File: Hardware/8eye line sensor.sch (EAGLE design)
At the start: 78 parts, among them U1 SX1509, U101 QRE1113, U102 QRE1113, U103 QRE1113, U104 QRE1113, U105 QRE1113, U106 QRE1113, U107 QRE1113, U108 QRE1113, U2 74AC125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

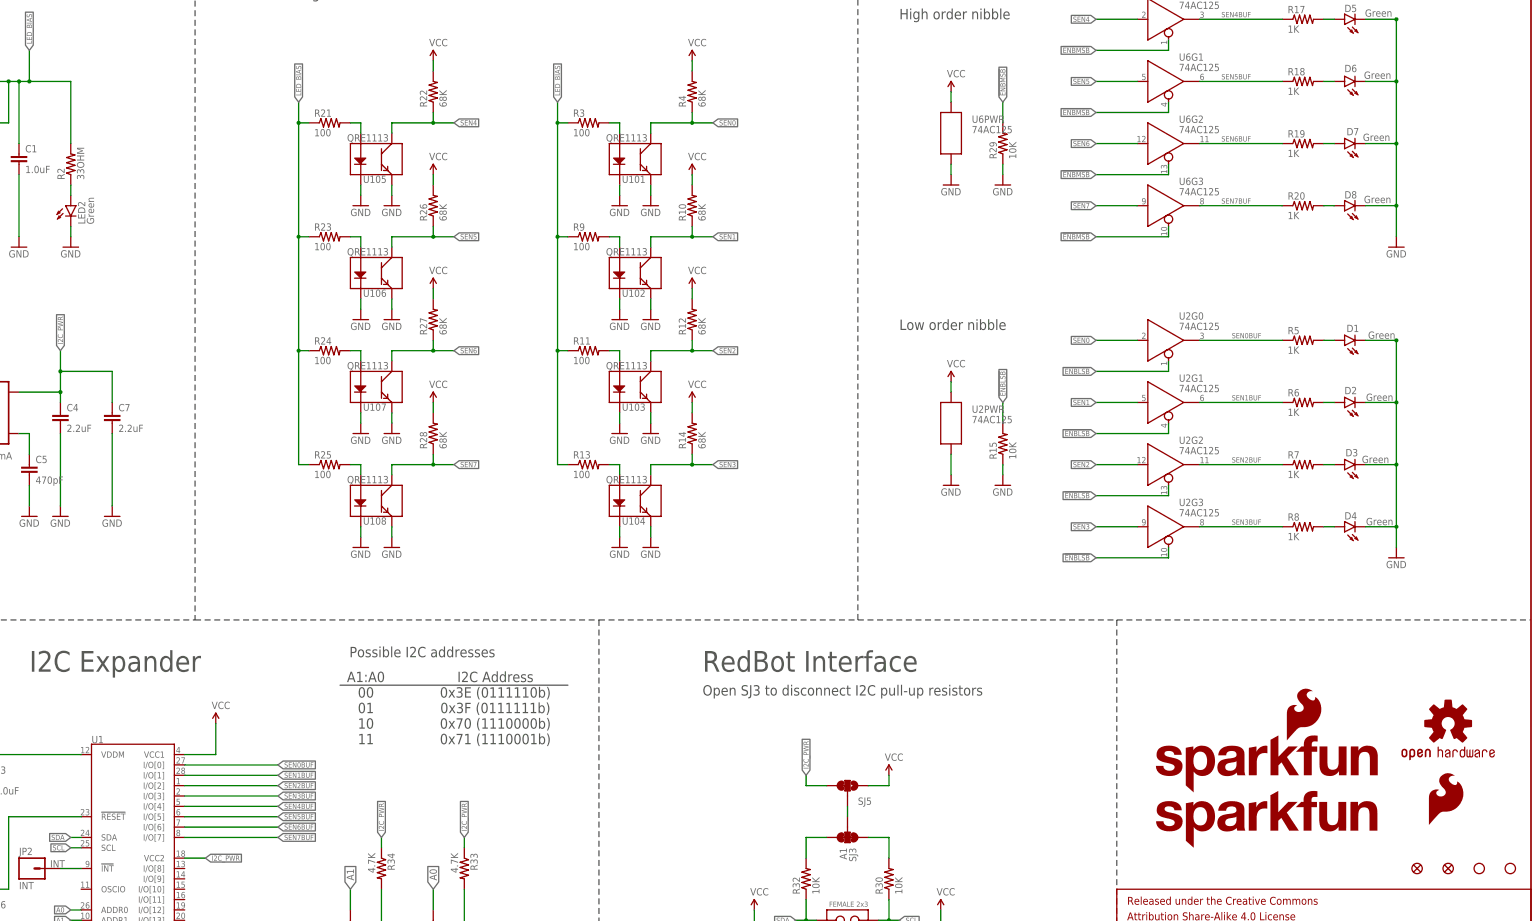
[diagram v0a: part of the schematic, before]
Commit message: Fixed github/qc finds
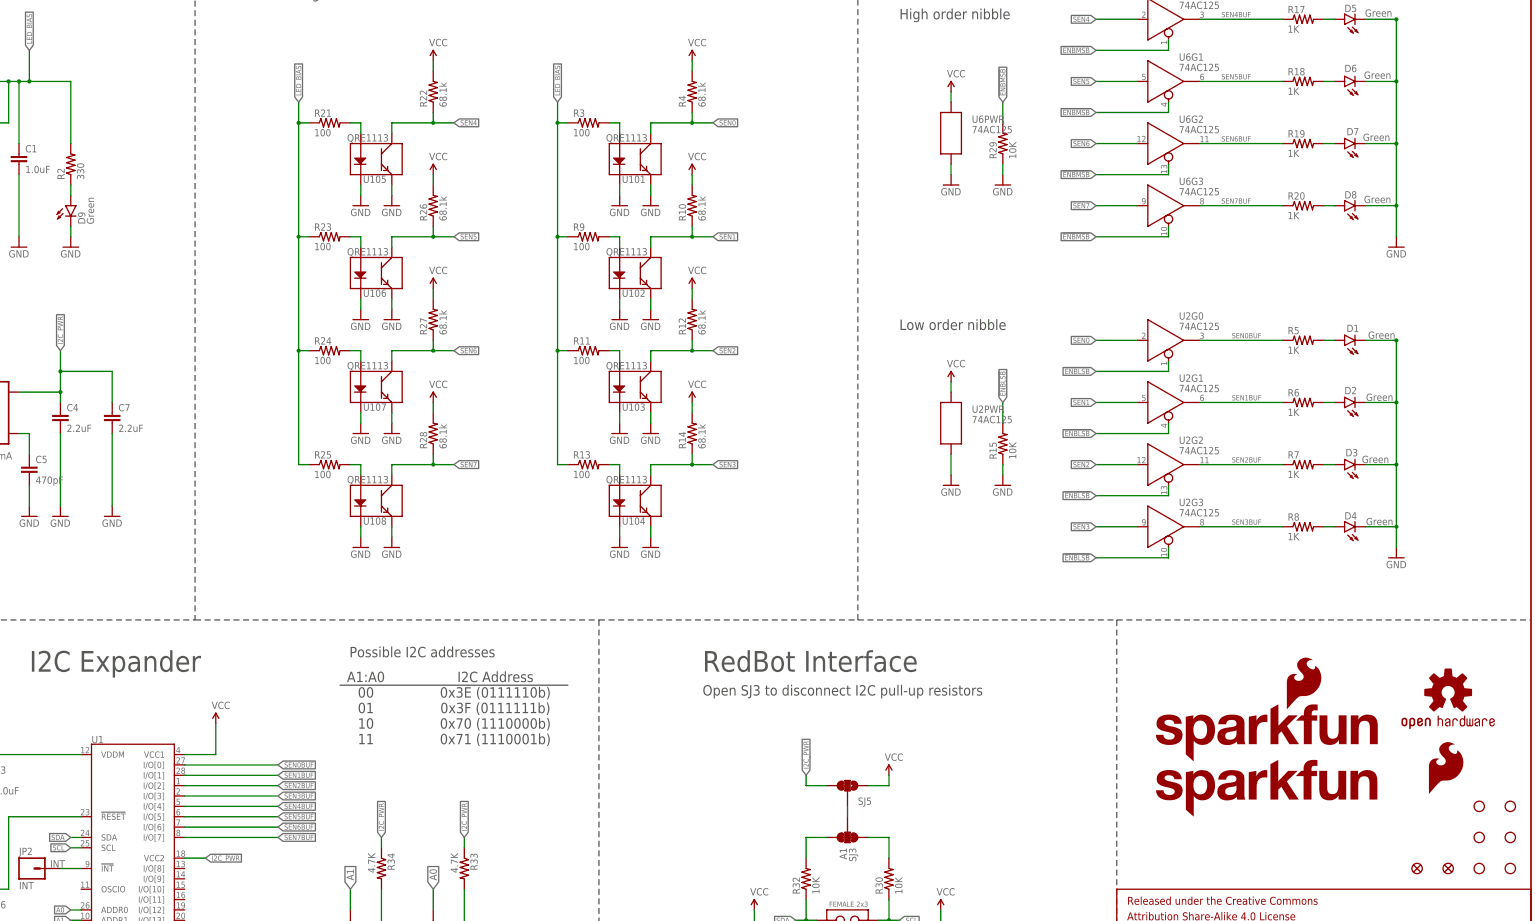
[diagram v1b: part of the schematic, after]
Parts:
- added STANDOFF1, STANDOFF2, STANDOFF5, STANDOFF6: STAND-OFF, SparkFun-Electromechanical:STAND-OFF
- R10, R12, R14, R22, R26, R27, R28, R4: value 68K -> 68.1k
- R2: value 33OHM -> 330; device SparkFun-Resistors:33OHM1/10W1%(0603) -> SparkFun-Resistors:330OHM1/10W1%(0603)
- renumbered LED2 to D9
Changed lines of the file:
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@@
 <part name="R1" library="SparkFun-Resistors" deviceset="4.7KOHM-1/10W-1%(0603)" device="" value="4.7K"/>
 <part name="R3" library="SparkFun-Resistors" deviceset="100OHM-1/10W-1%(0603)" device="" value="100"/>
-<part name="R4" library="SparkFun-Resistors" deviceset="68.1KOHM1/10W1%(0603)" device="" value="68K"/>
+<part name="R4" library="SparkFun-Resistors" deviceset="68.1KOHM1/10W1%(0603)" device="" value="68.1k"/>
 <part name="GND1" library="SparkFun-Aesthetics" deviceset="GND" device=""/>
 <part name="GND2" library="SparkFun-Aesthetics" deviceset="GND" device=""/>
@@
 <part name="GND12" library="SparkFun-Aesthetics" deviceset="GND" device=""/>
 <part name="SUPPLY2" library="SparkFun-Aesthetics" deviceset="VCC" device=""/>
-<part name="R10" library="SparkFun-Resistors" deviceset="68.1KOHM1/10W1%(0603)" device="" value="68K"/>
+<part name="R10" library="SparkFun-Resistors" deviceset="68.1KOHM1/10W1%(0603)" device="" value="68.1k"/>
 <part name="SUPPLY3" library="SparkFun-Aesthetics" deviceset="VCC" device=""/>
-<part name="R12" library="SparkFun-Resistors" deviceset="68.1KOHM1/10W1%(0603)" device="" value="68K"/>
+<part name="R12" library="SparkFun-Resistors" deviceset="68.1KOHM1/10W1%(0603)" device="" value="68.1k"/>
 <part name="SUPPLY4" library="SparkFun-Aesthetics" deviceset="VCC" device=""/>
-<part name="R14" library="SparkFun-Resistors" deviceset="68.1KOHM1/10W1%(0603)" device="" value="68K"/>
+<part name="R14" library="SparkFun-Resistors" deviceset="68.1KOHM1/10W1%(0603)" device="" value="68.1k"/>
 <part name="SUPPLY5" library="SparkFun-Aesthetics" deviceset="VCC" device=""/>
 <part name="SUPPLY6" library="SparkFun-Aesthetics" deviceset="VCC" device=""/>
@@
 <part name="R15" library="SparkFun-Resistors" deviceset="10KOHM-1/10W-1%(0603)" device="0603" value="10K"/>
 <part name="R16" library="SparkFun-Electromechanical" deviceset="TRIMPOT" device="-PTH-KNOB" value="TSR-3386"/>
-<part name="R2" library="SparkFun-Resistors" deviceset="33OHM1/10W1%(0603)" device="" value="33OHM"/>
-<part name="LED2" library="SparkFun-LED" deviceset="LED-GREEN" device="1206-BOTTOM" value="Green"/>
+<part name="R2" library="SparkFun-Resistors" deviceset="330OHM1/10W1%(0603)" device="" value="330"/>
+<part name="D9" library="SparkFun-LED" deviceset="LED-GREEN" device="1206-BOTTOM" value="Green"/>
 <part name="GND16" library="SparkFun" deviceset="GND" device=""/>
 <part name="GND17" library="SparkFun-Aesthetics" deviceset="GND" device=""/>
@@
 <part name="U105" library="SparkFun-Sensors" deviceset="QRE1113" device="" value="QRE1113"/>
 <part name="R21" library="SparkFun-Resistors" deviceset="100OHM-1/10W-1%(0603)" device="" value="100"/>
-<part name="R22" library="SparkFun-Resistors" deviceset="68.1KOHM1/10W1%(0603)" device="" value="68K"/>
+<part name="R22" library="SparkFun-Resistors" deviceset="68.1KOHM1/10W1%(0603)" device="" value="68.1k"/>
 <part name="GND19" library="SparkFun-Aesthetics" deviceset="GND" device=""/>
 <part name="GND20" library="SparkFun-Aesthetics" deviceset="GND" device=""/>
@@
 <part name="GND26" library="SparkFun-Aesthetics" deviceset="GND" device=""/>
 <part name="SUPPLY9" library="SparkFun-Aesthetics" deviceset="VCC" device=""/>
-<part name="R26" library="SparkFun-Resistors" deviceset="68.1KOHM1/10W1%(0603)" device="" value="68K"/>
+<part name="R26" library="SparkFun-Resistors" deviceset="68.1KOHM1/10W1%(0603)" device="" value="68.1k"/>
 <part name="SUPPLY10" library="SparkFun-Aesthetics" deviceset="VCC" device=""/>
-<part name="R27" library="SparkFun-Resistors" deviceset="68.1KOHM1/10W1%(0603)" device="" value="68K"/>
+<part name="R27" library="SparkFun-Resistors" deviceset="68.1KOHM1/10W1%(0603)" device="" value="68.1k"/>
 <part name="SUPPLY11" library="SparkFun-Aesthetics" deviceset="VCC" device=""/>
-<part name="R28" library="SparkFun-Resistors" deviceset="68.1KOHM1/10W1%(0603)" device="" value="68K"/>
+<part name="R28" library="SparkFun-Resistors" deviceset="68.1KOHM1/10W1%(0603)" device="" value="68.1k"/>
 <part name="SUPPLY12" library="SparkFun-Aesthetics" deviceset="VCC" device=""/>
 <part name="SJ1" library="SparkFun-Passives" deviceset="JUMPER-PAD-3-2OF3_NC_BY_PASTE" device="" value="A0"/>
@@
 <part name="FID1" library="SparkFun-Aesthetics" deviceset="FIDUCIAL" device="UFIDUCIAL"/>
 <part name="FID2" library="SparkFun-Aesthetics" deviceset="FIDUCIAL" device="UFIDUCIAL"/>
-<part name="STANDOFF3" library="SparkFun-Electromechanical" deviceset="STAND-OFF" device=""/>
-<part name="STANDOFF4" library="SparkFun-Electromechanical" deviceset="STAND-OFF" device=""/>
 <part name="U6" library="SparkFun-DigitalIC" deviceset="74*125" device="" technology="AC125DG" value="74AC125"/>
 <part name="U2" library="SparkFun-DigitalIC" deviceset="74*125" device="" technology="AC125DG" value="74AC125"/>
@@
 <part name="R34" library="SparkFun-Resistors" deviceset="4.7KOHM-1/10W-1%(0603)" device="" value="4.7K"/>
 <part name="LOGO1" library="SparkFun-Aesthetics" deviceset="SFE_LOGO_NAME_FLAME" device=".2_INCH"/>
+<part name="STANDOFF1" library="SparkFun-Electromechanical" deviceset="STAND-OFF" device=""/>
+<part name="STANDOFF2" library="SparkFun-Electromechanical" deviceset="STAND-OFF" device=""/>
+<part name="STANDOFF3" library="SparkFun-Electromechanical" deviceset="STAND-OFF" device=""/>
+<part name="STANDOFF4" library="SparkFun-Electromechanical" deviceset="STAND-OFF" device=""/>
+<part name="STANDOFF5" library="SparkFun-Electromechanical" deviceset="STAND-OFF" device=""/>
+<part name="STANDOFF6" library="SparkFun-Electromechanical" deviceset="STAND-OFF" device=""/>
 </parts>
 <sheets>
@@
 </instance>
 <instance part="R2" gate="G$1" x="73.66" y="213.36" rot="R90"/>
-<instance part="LED2" gate="G$1" x="73.66" y="203.2"/>
+<instance part="D9" gate="G$1" x="73.66" y="203.2"/>
 <instance part="GND16" gate="1" x="73.66" y="193.04"/>
 <instance part="GND17" gate="1" x="398.78" y="193.04"/>
@@
 <instance part="FRAME2" gate="G$2" x="330.2" y="0"/>
 <instance part="JP2" gate="G$1" x="63.5" y="40.64"/>
-<instance part="LOGO2" gate="G$1" x="337.82" y="45.72"/>
-<instance part="LOGO5" gate="G$1" x="406.4" y="50.8"/>
-<instance part="LOGO6" gate="G$1" x="411.48" y="76.2"/>
+<instance part="LOGO2" gate="G$1" x="337.82" y="53.34"/>
+<instance part="LOGO5" gate="G$1" x="406.4" y="58.42"/>
+<instance part="LOGO6" gate="G$1" x="411.48" y="83.82"/>
 <instance part="FID1" gate="G$1" x="403.86" y="40.64"/>
 <instance part="FID2" gate="G$1" x="411.48" y="40.64"/>
-<instance part="STANDOFF3" gate="G$1" x="419.1" y="40.64"/>
-<instance part="STANDOFF4" gate="G$1" x="426.72" y="40.64"/>
 <instance part="U6" gate="G0" x="340.36" y="248.92"/>
 <instance part="U6" gate="G1" x="340.36" y="233.68"/>
@@
 <instance part="R33" gate="G$1" x="170.18" y="40.64" rot="R270"/>
 <instance part="R34" gate="G$1" x="149.86" y="40.64" rot="R270"/>
-<instance part="LOGO1" gate="G$1" x="339.09" y="58.928"/>
+<instance part="LOGO1" gate="G$1" x="339.09" y="66.548"/>
+<instance part="STANDOFF1" gate="G$1" x="419.1" y="40.64"/>
+<instance part="STANDOFF2" gate="G$1" x="426.72" y="40.64"/>
+<instance part="STANDOFF3" gate="G$1" x="419.1" y="48.26"/>
+<instance part="STANDOFF4" gate="G$1" x="426.72" y="48.26"/>
+<instance part="STANDOFF5" gate="G$1" x="419.1" y="55.88"/>
+<instance part="STANDOFF6" gate="G$1" x="426.72" y="55.88"/>
 </instances>
 <busses>
@@
 <wire x1="73.66" y1="195.58" x2="73.66" y2="198.12" width="0.1524" layer="91"/>
 <pinref part="GND16" gate="1" pin="GND"/>
-<pinref part="LED2" gate="G$1" pin="C"/>
+<pinref part="D9" gate="G$1" pin="C"/>
 </segment>
 <segment>
@@
 <segment>
 <wire x1="73.66" y1="205.74" x2="73.66" y2="208.28" width="0.1524" layer="91"/>
-<pinref part="LED2" gate="G$1" pin="A"/>
+<pinref part="D9" gate="G$1" pin="A"/>
 <pinref part="R2" gate="G$1" pin="1"/>
 </segment>

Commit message: v04: IR LED power ctrl, regulated receiver supply
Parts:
- removed R15, R29: 10K, SparkFun-Resistors:10KOHM-1/10W-1%(0603)0603
- added C8: 10uF, SparkFun-Capacitors:10UF-16V-10%(TANT)
- added Q1: MOSFET-NCHANNEL2N7002PW, SparkFun-DiscreteSemi:MOSFET-NCHANNEL2N7002PW
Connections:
- removed net !ENBLSB: R15.2, U2G0.!EN, U2G1.!EN, U2G2.!EN, U2G3.!EN
- removed net !ENBMSB: R29.2, U6G0.!EN, U6G1.!EN, U6G2.!EN, U6G3.!EN
- new net !FBLEDEN: U1.I/O[9], U2G0.!EN, U2G1.!EN, U2G2.!EN, U2G3.!EN, U6G0.!EN, U6G1.!EN, U6G2.!EN, U6G3.!EN
- new net !IRLEDEN: Q1.G, U1.I/O[8]
- net GND: now also C8.-, Q1.S; no longer R15.1, R29.1
- net I2C_PWR: now also R10.2, R12.2, R14.2, R22.2, R26.2, R27.2, R28.2, R4.2, U1.VCC1, U2PWR.P$V+, U6PWR.P$V+
- net N$1: now also Q1.D
- net VCC: now also C8.+; no longer R10.2, R12.2, R14.2, R22.2, R26.2, R27.2, R28.2, R4.2, U1.VCC1, U2PWR.P$V+, U6PWR.P$V+
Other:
- note added: "Open SJ3 to disconnect I2C pull-up resistors Move SJ5 to make interface 5v"
- note added: "Set I2C address with SJ1 and SJ2"
- note added: "V04"
- note removed: "Open SJ3 to disconnect I2C pull-up resistors"
- note removed: "Set I2C addres with SJ1 and SJ2"
- note removed: "V03"
- moved on the sheet: C1, C4, C5, C7, D9, R16, R2, U3

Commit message: Fixed QC issues
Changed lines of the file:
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@@
 <text x="63.5" y="88.9" size="5.08" layer="97">I2C Expander</text>
 <text x="119.126" y="10.922" size="2.54" layer="97">Set I2C address with SJ1 and SJ2</text>
-<text x="228.6" y="83.058" size="2.54" layer="97">Open SJ3 to disconnect I2C pull-up resistors
+<text x="228.346" y="80.518" size="2.54" layer="97">Open SJ3 to disconnect I2C pull-up resistors
 Move SJ5 to make interface 5v</text>
 <text x="141.986" y="92.456" size="2.54" layer="97">Possible I2C addresses</text>
@@
 <instance part="STANDOFF5" gate="G$1" x="419.1" y="55.88"/>
 <instance part="STANDOFF6" gate="G$1" x="426.72" y="55.88"/>
-<instance part="Q1" gate="G$1" x="66.04" y="203.2"/>
+<instance part="Q1" gate="G$1" x="66.04" y="203.2" smashed="yes">
+<attribute name="NAME" x="64.516" y="196.85" size="1.778" layer="95" rot="R90"/>
+<attribute name="VALUE" x="71.882" y="194.056" size="1.778" layer="96" rot="R90"/>
+</instance>
 <instance part="GND38" gate="1" x="66.04" y="193.04"/>
 <instance part="C8" gate="G$1" x="17.78" y="215.9"/>

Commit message: V_1.0 update
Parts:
- R30, R32: value 10K -> 4.7K; device SparkFun-Resistors:10KOHM-1/10W-1%(0603)0603 -> SparkFun-Resistors:4.7KOHM-1/10W-1%(0603)
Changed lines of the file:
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@@
 <part name="GND28" library="SparkFun" deviceset="GND" device=""/>
 <part name="GND30" library="SparkFun" deviceset="GND" device=""/>
-<part name="R30" library="SparkFun-Resistors" deviceset="10KOHM-1/10W-1%(0603)" device="0603" value="10K"/>
+<part name="R30" library="SparkFun-Resistors" deviceset="4.7KOHM-1/10W-1%(0603)" device="" value="4.7K"/>
 <part name="GND15" library="SparkFun-Aesthetics" deviceset="GND" device=""/>
 <part name="SUPPLY7" library="SparkFun-Aesthetics" deviceset="VCC" device=""/>
-<part name="R32" library="SparkFun-Resistors" deviceset="10KOHM-1/10W-1%(0603)" device="0603" value="10K"/>
+<part name="R32" library="SparkFun-Resistors" deviceset="4.7KOHM-1/10W-1%(0603)" device="" value="4.7K"/>
 <part name="C3" library="SparkFun-Capacitors" deviceset="1.0UF-16V-10%(0603)" device="" value="1.0uF"/>
 <part name="U1" library="SparkFun-DigitalIC" deviceset="SX1509" device="" value="SX1509"/>

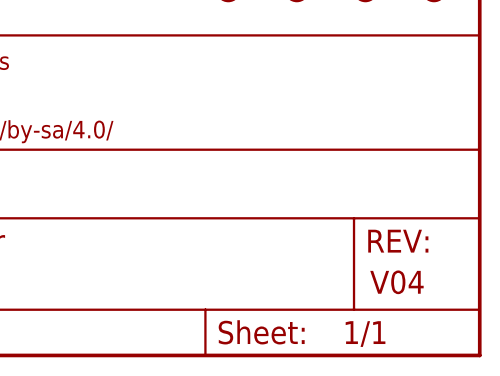
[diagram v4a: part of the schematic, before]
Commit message: Fixed rev number and readme
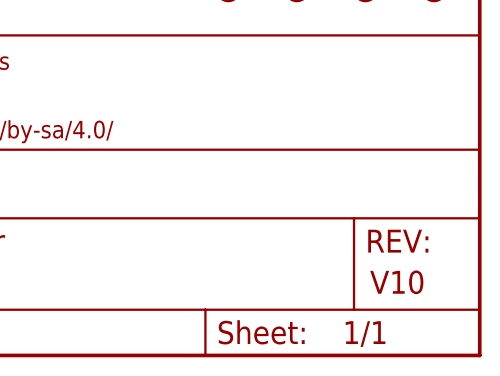
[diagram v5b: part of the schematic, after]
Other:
- note added: "V10"
- note removed: "V04"
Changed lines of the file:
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@@
 <plain>
 <text x="355.092" y="11.43" size="2.54" layer="94">Marshall Taylor</text>
-<text x="419.608" y="6.858" size="2.54" layer="94">V04</text>
+<text x="419.608" y="6.858" size="2.54" layer="94">V10</text>
 <text x="193.04" y="254" size="2.54" layer="97">Low order nibble</text>
 <text x="37.592" y="260.35" size="2.54" layer="97">Supply +5V</text>
